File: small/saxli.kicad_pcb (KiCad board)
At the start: 4 copper layers, 160.5 x 102.4 mm, 191 parts, among them IC1 PIC32MX350F256H-V_PT, IC2 SIM808, J1 78800-0001, J10 Conn_01x06_Female, J11 Conn_Coaxial, J12 Conn_Coaxial, J2 Screw_Terminal_01x02, J3 Micro_SD_Card, J4 Conn_01x05_Female, J5 Conn_02x04_Odd_Even, J6 RJ45_Amphenol_RJMG1BD3B8K1ANR, J7 Screw_Terminal_01x08, J8 Screw_Terminal_01x08, J9 Screw_Terminal_01x08, Q1 2N7002, Q2 2N7002, Q3 2N7002, U1 LM358, U10 TPS5430DDAR, U11 EL357N(C)(TA)-G, U12 EL357N(C)(TA)-G, U13 ASSR-1218, U14 ST485EBDR, U15 ASSR-1218, U16 SRV05-4, U18 ULN2003A, U2 LM7805_TO220, U20 TPS5430DDAR, U3 LD1117S33TR_SOT223, U4 ENC28J60x-SS, U5 AT25M02, U6 EL357N(C)(TA)-G, U7 EL357N(C)(TA)-G, U8 PCF8563T, U9 ISO1540, Y1 Crystal, Y2 Crystal

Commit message: Ethernet connector connection fix
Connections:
- J6 pad R1: /etherne/TPOUT- -> /etherne/TPOUT+
- J6 pad R2: /etherne/TPOUT+ -> /etherne/TPOUT-
- R20 pad 1: /etherne/TPOUT+ -> /etherne/TPOUT-
- R21 pad 1: /etherne/TPOUT- -> /etherne/TPOUT+
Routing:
- net /etherne/TPOUT+: track 25.5 -> 34.0 mm, vias 0 -> 3
- net /etherne/TPOUT-: track 31.2 -> 25.6 mm, vias 2 -> 0
- net VDD5: track 328.7 -> 333.4 mm, vias 10 -> 9
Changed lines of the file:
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@@
     (thickness 1.6)
     (drawings 7)
-    (tracks 2319)
+    (tracks 2327)
     (zones 0)
     (modules 191)
@@
     )
     (pad 1 smd roundrect (at -0.825 0 270) (size 0.8 0.95) (layers F.Cu F.Paste F.Mask) (roundrect_rratio 0.25)
-      (net 45 /etherne/TPOUT-))
+      (net 44 /etherne/TPOUT+))
     (pad 2 smd roundrect (at 0.825 0 270) (size 0.8 0.95) (layers F.Cu F.Paste F.Mask) (roundrect_rratio 0.25)
       (net 27 "Net-(C16-Pad2)"))
@@
     )
     (pad 1 smd roundrect (at -0.825 0 270) (size 0.8 0.95) (layers F.Cu F.Paste F.Mask) (roundrect_rratio 0.25)
-      (net 44 /etherne/TPOUT+))
+      (net 45 /etherne/TPOUT-))
     (pad 2 smd roundrect (at 0.825 0 270) (size 0.8 0.95) (layers F.Cu F.Paste F.Mask) (roundrect_rratio 0.25)
       (net 27 "Net-(C16-Pad2)"))
@@
       (net 43 /etherne/TPIN+))
     (pad R2 thru_hole circle (at 1.27 -2.54) (size 1.9 1.9) (drill 0.9) (layers *.Cu *.Mask)
-      (net 44 /etherne/TPOUT+))
-    (pad R1 thru_hole rect (at 0 0) (size 1.9 1.9) (drill 0.9) (layers *.Cu *.Mask)
       (net 45 /etherne/TPOUT-))
+    (pad R1 thru_hole rect (at 0 0) (size 1.9 1.9) (drill 0.9) (layers *.Cu *.Mask)
+      (net 44 /etherne/TPOUT+))
     (model ${KISYS3DMOD}/Connector_RJ.3dshapes/RJ45_Amphenol_RJMG1BD3B8K1ANR.wrl
       (at (xyz 0 0 0))
@@
   (segment (start 178.689 86.741) (end 177.74201 85.79401) (width 0.25) (layer F.Cu) (net 43))
   (segment (start 180.262 86.741) (end 178.689 86.741) (width 0.25) (layer F.Cu) (net 43))
-  (segment (start 182.372 91.377) (end 182.372 90.551) (width 0.25) (layer F.Cu) (net 44))
-  (segment (start 187.452 85.471) (end 189.562 85.471) (width 0.25) (layer F.Cu) (net 44))
-  (segment (start 182.372 90.551) (end 183.388 89.535) (width 0.25) (layer F.Cu) (net 44))
-  (segment (start 183.388 89.535) (end 187.452 85.471) (width 0.25) (layer F.Cu) (net 44))
-  (segment (start 175.26 92.837) (end 176.72 91.377) (width 0.25) (layer F.Cu) (net 44))
-  (segment (start 182.372 91.377) (end 176.72 91.377) (width 0.25) (layer F.Cu) (net 44))
-  (segment (start 175.26 100.457) (end 175.26 92.837) (width 0.25) (layer F.Cu) (net 44))
-  (segment (start 173.984999 102.991999) (end 173.984999 92.715001) (width 0.25) (layer F.Cu) (net 45))
-  (segment (start 173.99 102.997) (end 173.984999 102.991999) (width 0.25) (layer F.Cu) (net 45))
-  (segment (start 184.277 91.377) (end 184.277 91.186) (width 0.25) (layer F.Cu) (net 45))
+  (segment (start 175.26 92.837) (end 176.72 91.377) (width 0.25) (layer F.Cu) (net 45))
+  (segment (start 182.372 91.377) (end 176.72 91.377) (width 0.25) (layer F.Cu) (net 45))
+  (segment (start 175.26 100.457) (end 175.26 92.837) (width 0.25) (layer F.Cu) (net 45))
+  (segment (start 173.984999 102.991999) (end 173.984999 92.715001) (width 0.25) (layer F.Cu) (net 44))
+  (segment (start 173.99 102.997) (end 173.984999 102.991999) (width 0.25) (layer F.Cu) (net 44))
+  (segment (start 184.277 91.377) (end 184.277 91.186) (width 0.25) (layer F.Cu) (net 44))
   (segment (start 188.722 86.741) (end 189.562 86.741) (width 0.25) (layer F.Cu) (net 45))
-  (segment (start 184.277 91.186) (end 185.928 89.535) (width 0.25) (layer F.Cu) (net 45))
-  (segment (start 185.928 89.535) (end 188.722 86.741) (width 0.25) (layer F.Cu) (net 45))
-  (via (at 185.928 89.535) (size 0.8) (drill 0.4) (layers F.Cu B.Cu) (net 45))
-  (via (at 173.984999 92.715001) (size 0.8) (drill 0.4) (layers F.Cu B.Cu) (net 45))
-  (segment (start 173.984999 92.715001) (end 183.382999 92.715001) (width 0.25) (layer In2.Cu) (net 45))
-  (segment (start 185.928 90.17) (end 185.928 89.535) (width 0.25) (layer In2.Cu) (net 45))
-  (segment (start 183.382999 92.715001) (end 185.928 90.17) (width 0.25) (layer In2.Cu) (net 45))
+  (segment (start 184.277 91.186) (end 185.928 89.535) (width 0.25) (layer F.Cu) (net 44))
+  (via (at 185.928 89.535) (size 0.8) (drill 0.4) (layers F.Cu B.Cu) (net 44))
+  (via (at 173.984999 92.715001) (size 0.8) (drill 0.4) (layers F.Cu B.Cu) (net 44))
+  (segment (start 173.984999 92.715001) (end 183.382999 92.715001) (width 0.25) (layer In2.Cu) (net 44))
+  (segment (start 185.928 90.17) (end 185.928 89.535) (width 0.25) (layer In2.Cu) (net 44))
+  (segment (start 183.382999 92.715001) (end 185.928 90.17) (width 0.25) (layer In2.Cu) (net 44))
+  (segment (start 189.562 85.471) (end 186.182 85.471) (width 0.25) (layer F.Cu) (net 44))
+  (segment (start 186.182 85.471) (end 186.182 85.471) (width 0.25) (layer F.Cu) (net 44))
+  (via (at 186.182 85.471) (size 0.5) (drill 0.3) (layers F.Cu B.Cu) (net 44))
+  (segment (start 185.928 85.725) (end 186.182 85.471) (width 0.25) (layer In1.Cu) (net 44))
+  (segment (start 185.928 89.535) (end 185.928 85.725) (width 0.25) (layer In1.Cu) (net 44))
+  (segment (start 182.372 91.377) (end 182.372 90.805) (width 0.25) (layer F.Cu) (net 45))
+  (segment (start 186.436 86.741) (end 189.562 86.741) (width 0.25) (layer F.Cu) (net 45))
+  (segment (start 182.372 90.805) (end 186.436 86.741) (width 0.25) (layer F.Cu) (net 45))
   (segment (start 115.443 98.552) (end 115.443 95.44) (width 0.5) (layer F.Cu) (net 46))
   (segment (start 172.593 81.534) (end 172.529 81.534) (width 0.25) (layer F.Cu) (net 47))
@@
   (segment (start 131.1675 51.1575) (end 132.461 51.1575) (width 0.5) (layer F.Cu) (net 58))
   (via (at 131.191 49.022) (size 0.5) (drill 0.3) (layers F.Cu B.Cu) (net 58))
-  (segment (start 129.921 51.1575) (end 95.6545 51.1575) (width 0.25) (layer F.Cu) (net 58))
   (segment (start 95.7815 51.1575) (end 93.472 53.467) (width 0.5) (layer F.Cu) (net 58))
   (segment (start 168.783 94.804) (end 170.372 94.804) (width 0.25) (layer F.Cu) (net 58))
@@
   (segment (start 88.265 53.975) (end 93.091 53.975) (width 1.5) (layer B.Cu) (net 58))
   (segment (start 93.091 53.975) (end 93.091 53.975) (width 1.5) (layer B.Cu) (net 58))
-  (via (at 93.091 53.848) (size 0.5) (drill 0.3) (layers F.Cu B.Cu) (net 58))
   (segment (start 93.472 53.467) (end 93.0275 53.9115) (width 0.5) (layer F.Cu) (net 58))
-  (via (at 93.472 53.467) (size 0.5) (drill 0.3) (layers F.Cu B.Cu) (net 58))
+  (segment (start 93.0275 53.9115) (end 93.2815 53.9115) (width 0.5) (layer F.Cu) (net 58))
+  (segment (start 93.2815 53.9115) (end 93.345 53.975) (width 0.5) (layer F.Cu) (net 58))
+  (segment (start 93.345 53.975) (end 93.472 54.102) (width 0.5) (layer F.Cu) (net 58))
+  (via (at 93.345 53.975) (size 1) (drill 0.6) (layers F.Cu B.Cu) (net 58))
+  (segment (start 96.1625 51.1575) (end 96.3695 51.1575) (width 1) (layer F.Cu) (net 58))
+  (segment (start 93.345 53.975) (end 96.1625 51.1575) (width 1) (layer F.Cu) (net 58))
+  (segment (start 96.3695 51.1575) (end 95.6545 51.1575) (width 0.25) (layer F.Cu) (net 58))
+  (segment (start 129.921 51.1575) (end 96.3695 51.1575) (width 0.25) (layer F.Cu) (net 58))
   (segment (start 175.188012 79.11901) (end 173.86101 79.11901) (width 0.25) (layer F.Cu) (net 59))
   (segment (start 175.388002 79.319) (end 175.188012 79.11901) (width 0.25) (layer F.Cu) (net 59))

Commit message: sdcard and clock capacitor added.
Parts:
- added C52: 10uF, Capacitor_SMD:C_1206_3216Metric, F.Cu at (103.4, 46.5)
- added C53: 0.1u, Capacitor_SMD:C_0603_1608Metric, F.Cu at (129.8, 66.7)
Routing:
- net VDD3: track 555.9 -> 572.0 mm
- net GND: track 1159.1 -> 1174.6 mm
- net Net-(C53-Pad1): track 14.9 -> 16.4 mm

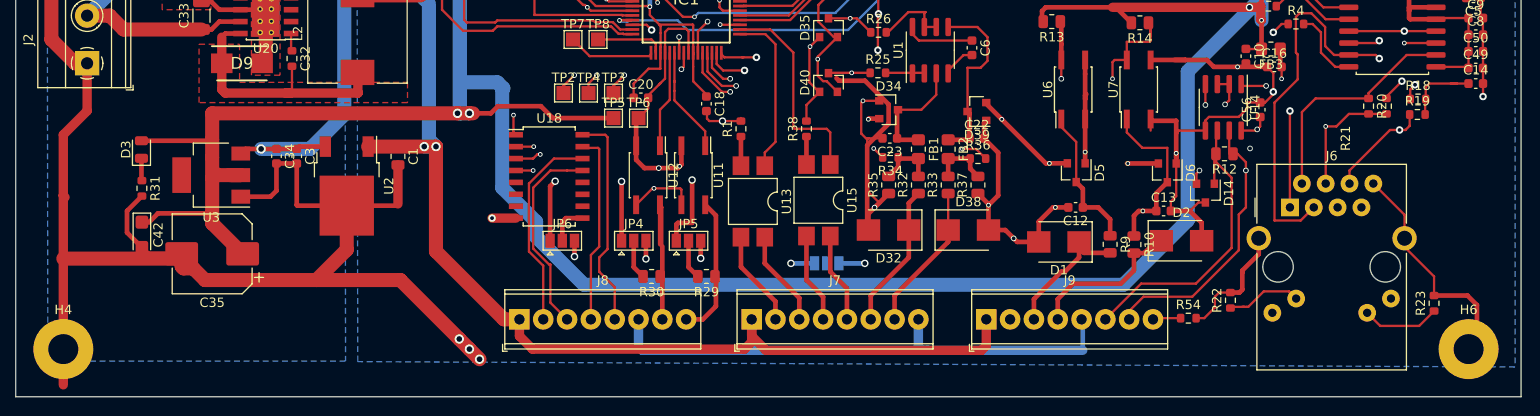
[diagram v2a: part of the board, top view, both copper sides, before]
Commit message: 3.3V changed to basic part.
thermal vias added for 5V regulator
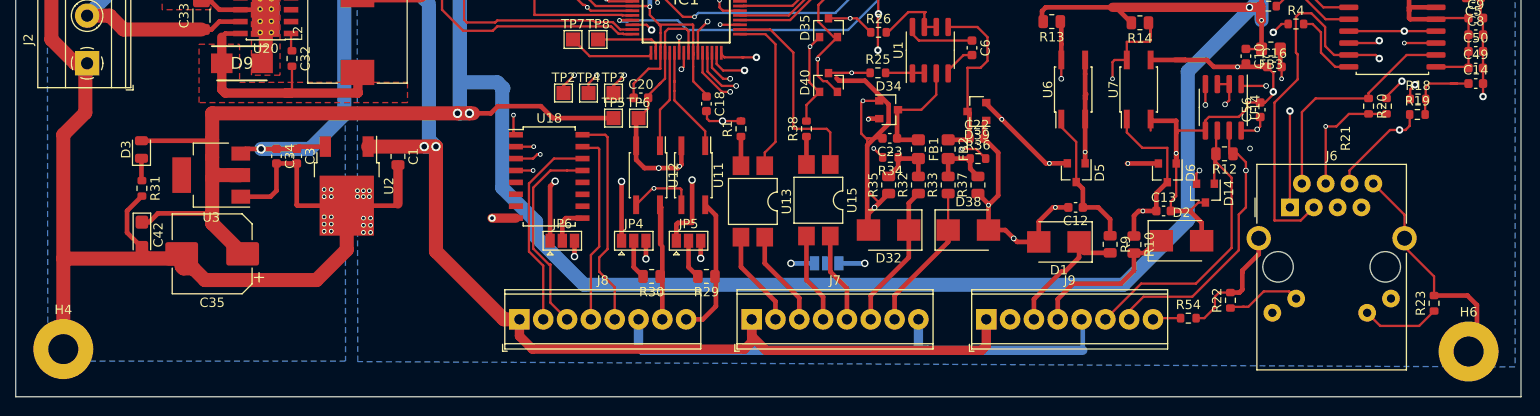
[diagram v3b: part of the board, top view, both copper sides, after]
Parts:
- moved H6 0.25 mm to (193.0, 118.4)
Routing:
- net GND: track 1174.6 -> 1163.1 mm, vias 46 -> 65
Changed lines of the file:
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@@
     (thickness 1.6)
     (drawings 7)
-    (tracks 2342)
+    (tracks 2358)
     (zones 0)
     (modules 193)
@@
   )
   (setup
-    (last_trace_width 0.25)
+    (last_trace_width 1.5)
     (user_trace_width 0.5)
     (user_trace_width 1)
@@
   )
   (module MountingHole:MountingHole_3.2mm_M3_Pad (layer F.Cu)
-    (at 193.04 118.11)
+    (at 193.04 118.364)
     (descr "Mounting Hole 3.2mm, M3")
     (tags "mounting hole 3.2mm m3")
@@
   (gr_line (start 198.628 20.828) (end 198.628 123.19) (layer Edge.Cuts) (width 0.05))
   (gr_line (start 38.1 20.828) (end 198.628 20.828) (layer Edge.Cuts) (width 0.05))
+  (via (at 74.549 101.219) (size 0.5) (drill 0.3) (layers F.Cu B.Cu) (net 1))
+  (via (at 74.549 101.854) (size 0.5) (drill 0.3) (layers F.Cu B.Cu) (net 1))
+  (via (at 75.819 101.219) (size 0.5) (drill 0.3) (layers F.Cu B.Cu) (net 1))
+  (via (at 75.184 101.219) (size 0.5) (drill 0.3) (layers F.Cu B.Cu) (net 1))
+  (via (at 75.819 101.854) (size 0.5) (drill 0.3) (layers F.Cu B.Cu) (net 1))
+  (via (at 75.184 101.854) (size 0.5) (drill 0.3) (layers F.Cu B.Cu) (net 1))
+  (via (at 75.946 104.14) (size 0.5) (drill 0.3) (layers F.Cu B.Cu) (net 1))
+  (via (at 75.184 104.14) (size 0.5) (drill 0.3) (layers F.Cu B.Cu) (net 1))
+  (via (at 75.946 104.902) (size 0.5) (drill 0.3) (layers F.Cu B.Cu) (net 1))
+  (via (at 75.184 104.902) (size 0.5) (drill 0.3) (layers F.Cu B.Cu) (net 1))
+  (via (at 75.184 105.664) (size 0.5) (drill 0.3) (layers F.Cu B.Cu) (net 1))
+  (via (at 75.946 105.664) (size 0.5) (drill 0.3) (layers F.Cu B.Cu) (net 1))
+  (via (at 71.755 101.854) (size 0.5) (drill 0.3) (layers F.Cu B.Cu) (net 1))
+  (via (at 71.755 101.092) (size 0.5) (drill 0.3) (layers F.Cu B.Cu) (net 1))
+  (via (at 70.993 101.092) (size 0.5) (drill 0.3) (layers F.Cu B.Cu) (net 1))
+  (via (at 70.993 101.854) (size 0.5) (drill 0.3) (layers F.Cu B.Cu) (net 1))
+  (via (at 71.755 104.013) (size 0.5) (drill 0.3) (layers F.Cu B.Cu) (net 1))
+  (via (at 71.755 104.775) (size 0.5) (drill 0.3) (layers F.Cu B.Cu) (net 1))
+  (via (at 71.755 105.537) (size 0.5) (drill 0.3) (layers F.Cu B.Cu) (net 1))
+  (via (at 70.993 104.013) (size 0.5) (drill 0.3) (layers F.Cu B.Cu) (net 1))
+  (via (at 70.993 104.775) (size 0.5) (drill 0.3) (layers F.Cu B.Cu) (net 1))
+  (via (at 70.993 105.537) (size 0.5) (drill 0.3) (layers F.Cu B.Cu) (net 1))
   (segment (start 60.198 49.784) (end 64.897 49.784) (width 1.5) (layer F.Cu) (net 1))
   (segment (start 62.197 53.594) (end 64.262 53.594) (width 0.5) (layer F.Cu) (net 1))
@@
   (segment (start 64.507 57.724) (end 64.507 59.309) (width 0.25) (layer F.Cu) (net 1))
   (segment (start 66.485 49.403) (end 65.278 49.403) (width 0.5) (layer F.Cu) (net 1))
-  (segment (start 45.72 92.71) (end 45.72 87.63) (width 1) (layer F.Cu) (net 1))
-  (segment (start 43.18 95.25) (end 45.72 92.71) (width 1) (layer F.Cu) (net 1))
   (segment (start 64.77 82.55) (end 64.77 78.105) (width 1.5) (layer F.Cu) (net 1))
   (segment (start 64.135 81.915) (end 64.77 82.55) (width 0.5) (layer F.Cu) (net 1))
@@
   (segment (start 43.18 108.458) (end 55.297 108.458) (width 1.5) (layer F.Cu) (net 1))
   (segment (start 43.18 108.458) (end 43.18 101.727) (width 1) (layer F.Cu) (net 1))
-  (segment (start 70.173 110.744) (end 79.121 110.744) (width 1.5) (layer F.Cu) (net 1))
-  (segment (start 79.121 110.744) (end 85.4075 117.0305) (width 1.5) (layer F.Cu) (net 1))
-  (segment (start 85.4075 117.0305) (end 86.487 118.11) (width 1.5) (layer F.Cu) (net 1))
-  (via (at 85.4075 117.0305) (size 1) (drill 0.6) (layers F.Cu B.Cu) (net 1))
-  (segment (start 86.487 118.11) (end 87.5665 119.1895) (width 1.5) (layer F.Cu) (net 1))
-  (via (at 86.487 118.11) (size 1) (drill 0.6) (layers F.Cu B.Cu) (net 1))
-  (via (at 87.5665 119.1895) (size 1) (drill 0.6) (layers F.Cu B.Cu) (net 1))
   (segment (start 101.35 81.022) (end 100.851 80.523) (width 0.25) (layer F.Cu) (net 1))
   (segment (start 100.851 80.523) (end 100.851 79.629) (width 0.25) (layer F.Cu) (net 1))
@@
   (segment (start 128.670747 89.488001) (end 125.896992 89.488001) (width 0.5) (layer F.Cu) (net 1))
   (segment (start 131.19299 92.010244) (end 128.670747 89.488001) (width 0.5) (layer F.Cu) (net 1))
-  (segment (start 43.18 121.92) (end 43.18 108.458) (width 1) (layer F.Cu) (net 1))
   (segment (start 134.366 117.983) (end 134.366 114.935) (width 1) (layer B.Cu) (net 1))
   (segment (start 134.62 118.237) (end 134.366 117.983) (width 1) (layer B.Cu) (net 1))
@@
   (segment (start 93.793 50.105) (end 93.793 47.685) (width 0.25) (layer F.Cu) (net 1))
   (segment (start 94.361 50.673) (end 93.793 50.105) (width 0.25) (layer F.Cu) (net 1))
+  (segment (start 43.18 95.25) (end 45.5295 92.9005) (width 1.5) (layer F.Cu) (net 1))
+  (segment (start 43.18 118.11) (end 43.18 95.25) (width 1.5) (layer F.Cu) (net 1))
+  (segment (start 45.5295 87.8205) (end 45.72 87.63) (width 1.5) (layer F.Cu) (net 1))
+  (segment (start 45.5295 92.9005) (end 45.5295 87.8205) (width 1.5) (layer F.Cu) (net 1))
   (segment (start 57.912 84.025) (end 58.977 84.025) (width 0.5) (layer F.Cu) (net 2))
   (segment (start 58.977 84.025) (end 59.817 83.185) (width 0.5) (layer F.Cu) (net 2))

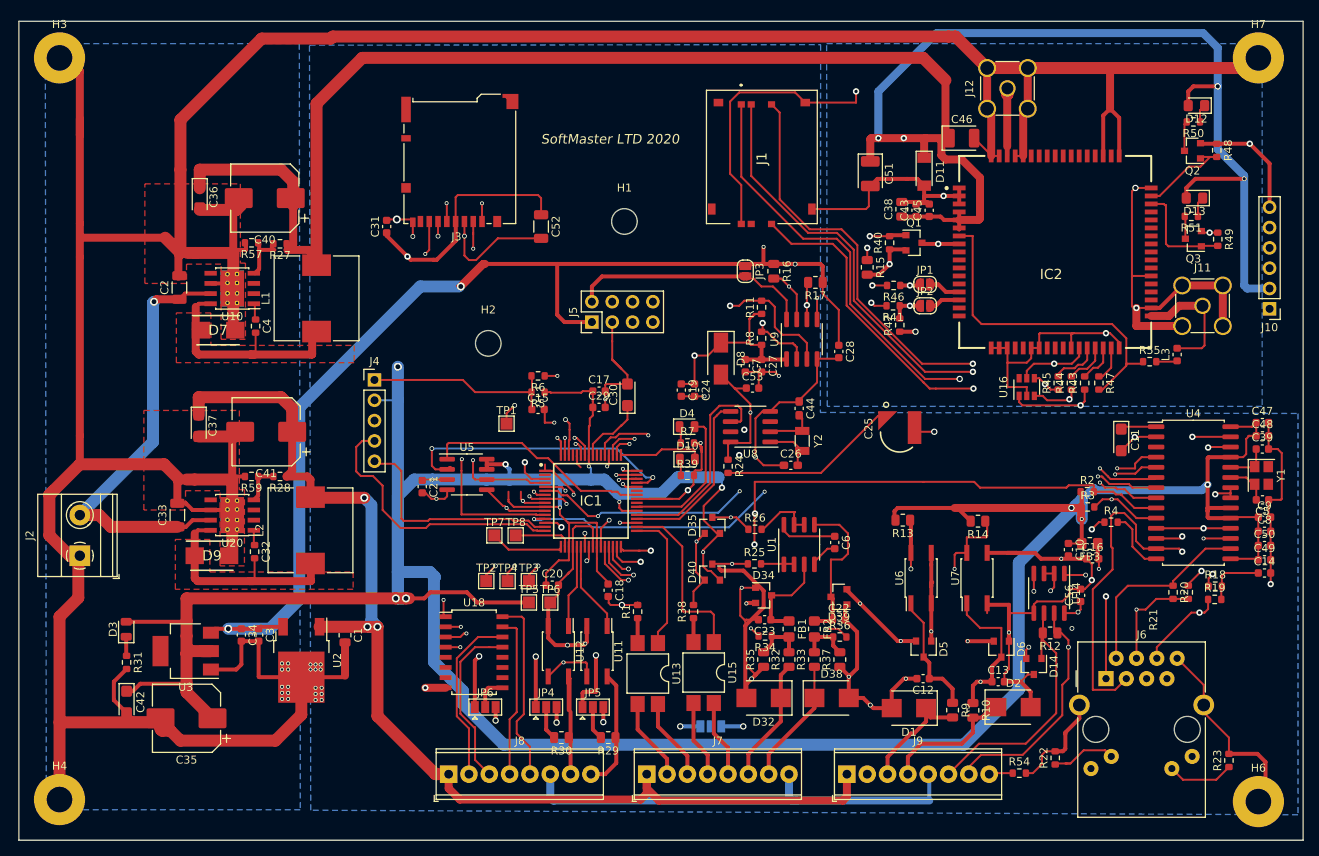
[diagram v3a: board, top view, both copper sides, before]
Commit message: capacitor added to sd card
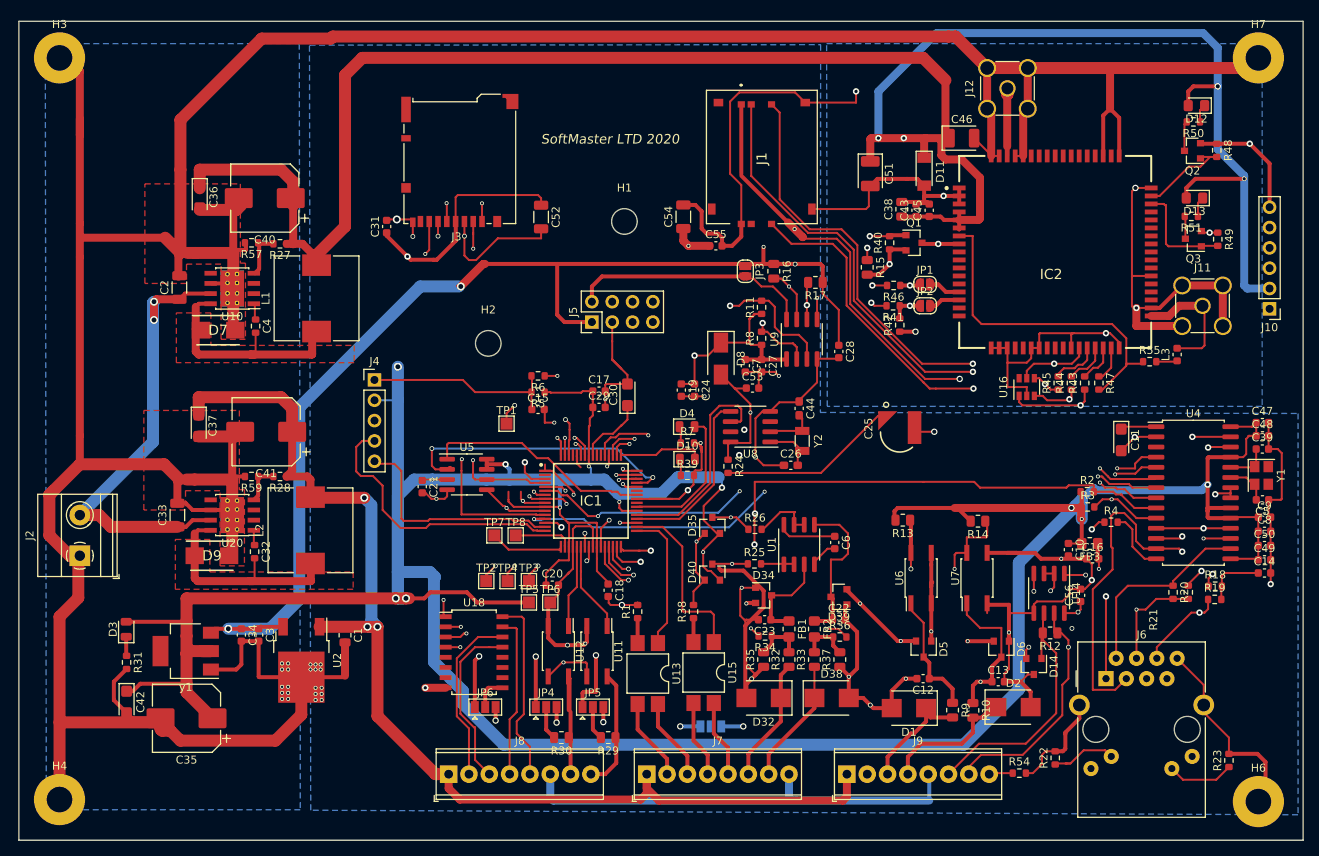
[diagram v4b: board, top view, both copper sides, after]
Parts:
- added C54: 10uF, Capacitor_SMD:C_1206_3216Metric, F.Cu at (121.2, 45.3)
- added C55: 0.1u, Capacitor_SMD:C_0603_1608Metric, F.Cu at (125.2, 48.9)
- у1: renamed from U3; value LD1117S33TR_SOT223 -> AMS1117-3.3
- moved C52 1.19 mm to (103.4, 45.3)
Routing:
- net /sim868/SIM_VDD: track 73.5 -> 95.4 mm, vias 2 -> 4
- net GND: track 1163.1 -> 1177.6 mm
- net 24Vin: track 55.3 -> 57.6 mm, vias 1 -> 2
- net VDD3: track 572.0 -> 570.8 mm
- net POWER_SIM: track 281.7 -> 280.5 mm
- net Net-(R27-Pad2): track 6.83 -> 5.86 mm
